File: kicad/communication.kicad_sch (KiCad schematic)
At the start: 34 parts, among them J1 CAN1A, J10 Debug, J2 CAN1B, J6 CAN0A, J7 CAN0B, U13 SK9822-EC20, U15 TJA1462ATK, U8 TJA1462ATK

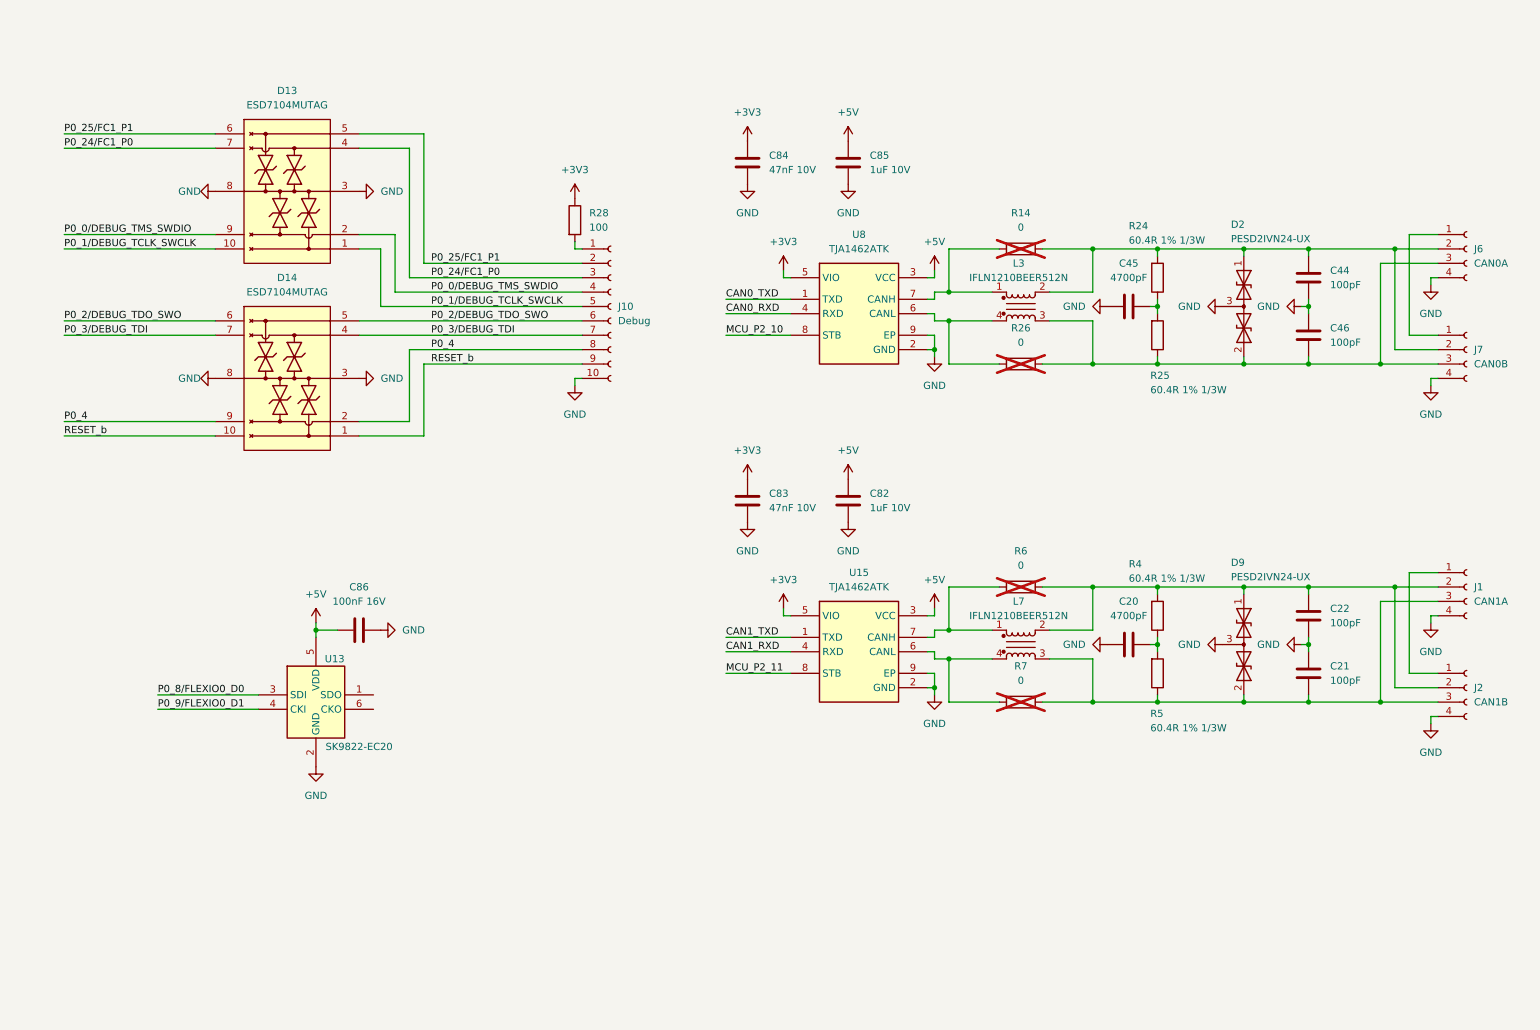
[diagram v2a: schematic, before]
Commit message: Updated schematic and started on layout
- Implemented schematic changes after feedback:
	- BMM350 VDD is 1.8V
	- Replaced net labels with global labels for page references
	- Added 1uF cap to SK9822-EC20
- Added rev-RMII configuration for TJA1103 and DNP resistor to put it in slave mode
- Added TJA1103 PHY address info
- Changed decoupling caps for MCXN to smallest possible packages
- Added traces and vias at MCXN according to guidelines
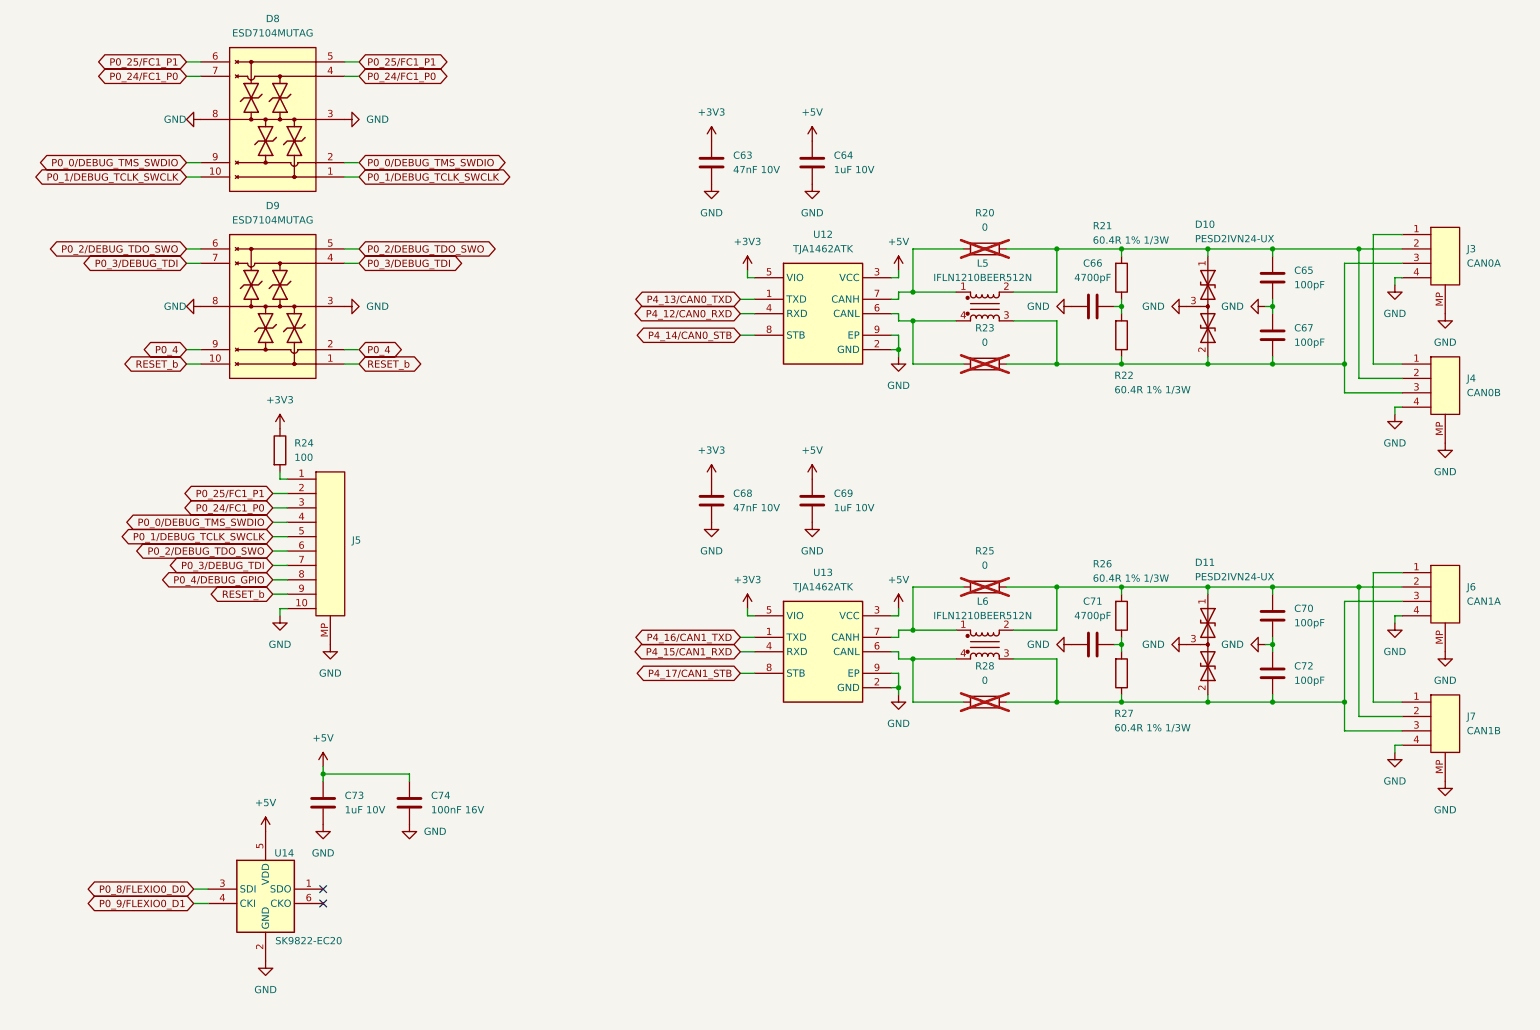
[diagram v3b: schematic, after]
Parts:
- removed J1: CAN1A, Connector_JST:JST_GH_SM04B-GHS-TB_1x04-1MP_P1.25mm_Horizontal, symbol Connector:Conn_01x04_Socket
- removed J10: Debug, Connector_JST:JST_SH_SM10B-SRSS-TB_1x10-1MP_P1.00mm_Horizontal, symbol Connector:Conn_01x10_Socket
- removed J2: CAN1B, Connector_JST:JST_GH_SM04B-GHS-TB_1x04-1MP_P1.25mm_Horizontal, symbol Connector:Conn_01x04_Socket
- removed J6: CAN0A, Connector_JST:JST_GH_SM04B-GHS-TB_1x04-1MP_P1.25mm_Horizontal, symbol Connector:Conn_01x04_Socket
- removed J7: CAN0B, Connector_JST:JST_GH_SM04B-GHS-TB_1x04-1MP_P1.25mm_Horizontal, symbol Connector:Conn_01x04_Socket
- added C73: 1uF 10V, Capacitor_SMD:C_0603_1608Metric, symbol Device:C
- added J3: CAN0A, Connector_JST:JST_GH_SM04B-GHS-TB_1x04-1MP_P1.25mm_Horizontal, symbol Connectors:JST_GH_SM04B-GHS-TB
- added J4: CAN0B, Connector_JST:JST_GH_SM04B-GHS-TB_1x04-1MP_P1.25mm_Horizontal, symbol Connectors:JST_GH_SM04B-GHS-TB
- added J5: ~, Connector_JST:JST_SH_SM10B-SRSS-TB_1x10-1MP_P1.00mm_Horizontal, symbol Connectors:JST_SH_SM10B-SRSS-TB
- added J6: CAN1A, Connector_JST:JST_GH_SM04B-GHS-TB_1x04-1MP_P1.25mm_Horizontal, symbol Connectors:JST_GH_SM04B-GHS-TB
- added J7: CAN1B, Connector_JST:JST_GH_SM04B-GHS-TB_1x04-1MP_P1.25mm_Horizontal, symbol Connectors:JST_GH_SM04B-GHS-TB
- renumbered C84 to C63, C85 to C64, C44 to C65, C45 to C66, C46 to C67, C83 to C68, C82 to C69, C22 to C70, C20 to C71, C21 to C72, C86 to C74, D2 to D10, D9 to D11, D13 to D8, D14 to D9, L3 to L5, L7 to L6, R14 to R20, R24 to R21, R25 to R22, R26 to R23, R28 to R24, R6 to R25, R4 to R26, R5 to R27, R7 to R28, U8 to U12, U15 to U13, U13 to U14
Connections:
- net +5V: now also C74.2, C73.2; no longer C74.1
- net GND: now also C74.1, C73.1, J3.4 (1), J3.MP, J4.4 (1), J4.MP, J5.10 (1), J5.MP, J6.4 (1), J6.MP, J7.4 (1), J7.MP; no longer C74.2
- net P0_0/DEBUG_TMS_SWDIO: now also J5.4 (1)
- net P0_1/DEBUG_TCLK_SWCLK: now also J5.5 (1)
- net P0_24/FC1_P0: now also J5.3 (1)
- net P0_25/FC1_P1: now also J5.2 (1)
- net P0_2/DEBUG_TDO_SWO: now also J5.6 (1)
- net P0_3/DEBUG_TDI: now also J5.7 (1)
- net RESET_b: now also J5.9 (1)
- net at C70.2, D11.1 (A1), L6.2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: now also J6.2 (1), J7.2 (1)
- net at C67.1, D10.2 (A2), L5.3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: now also J3.3 (1), J4.3 (1)
- net at C72.1, D11.2 (A2), L6.3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: now also J6.3 (1), J7.3 (1)
- net at C65.2, D10.1 (A1), L5.2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: now also J3.2 (1), J4.2 (1)
- net at R24.2: now also J5.1
- net CAN0_RXD renamed P4_12/CAN0_RXD
- net CAN0_TXD renamed P4_13/CAN0_TXD
- net CAN1_RXD renamed P4_15/CAN1_RXD
- net CAN1_TXD renamed P4_16/CAN1_TXD
- net MCU_P2_10 renamed P4_14/CAN0_STB
- net MCU_P2_11 renamed P4_17/CAN1_STB
- new net: J3.1, J4.1
- new net: J6.1, J7.1
- new net P0_4/DEBUG_GPIO: J5.8 (1)
- no-connect marks 0 -> 2
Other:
- moved on the sheet: C63, C64, C65, C66, C67, C68, C69, C70, C71, C72, C74, D10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

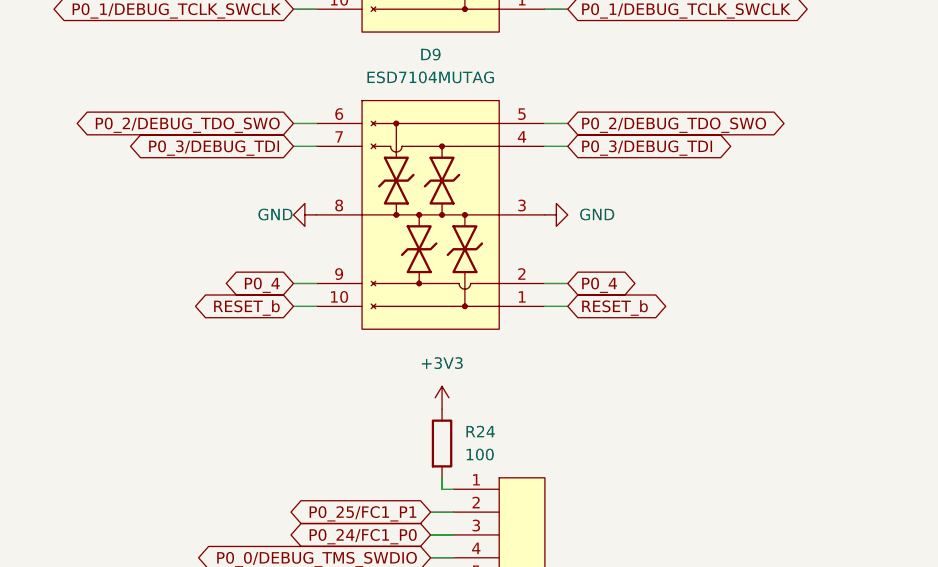
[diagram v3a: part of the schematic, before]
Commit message: Updated PCB layout
- Placed decoupling caps at MCXN with traces.
- Grouped parts of schematic.
- Started positioning Power components
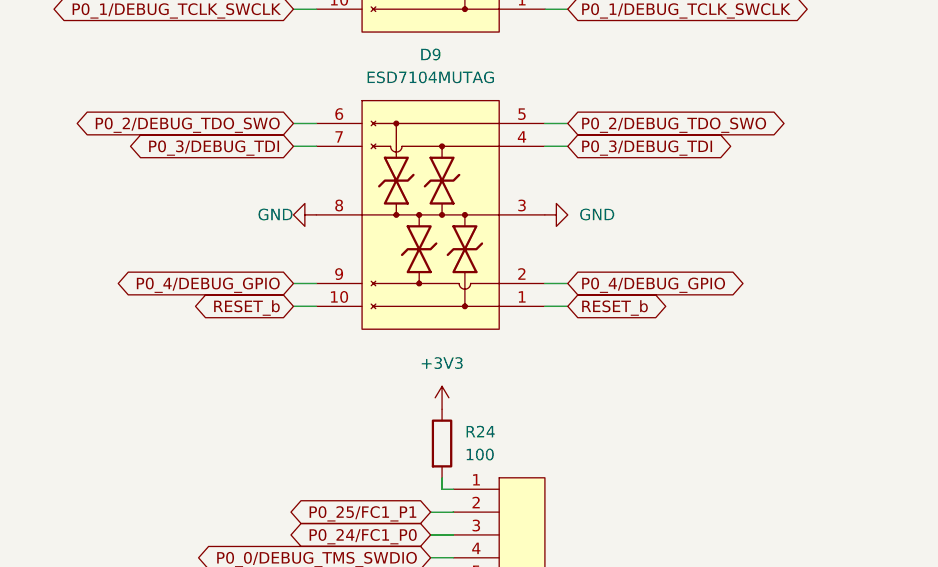
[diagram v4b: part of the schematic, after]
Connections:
- net P0_4 is gone; now on net P0_4/DEBUG_GPIO: D9.2 (IO_2), D9.9 (NC_3)
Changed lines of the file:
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@@
 		)
 	)
-	(global_label "P0_4"
+	(global_label "P4_12{slash}CAN0_RXD"
+		(shape bidirectional)
+		(at 144.78 67.31 180)
+		(fields_autoplaced yes)
+		(effects
+			(font
+				(size 1.27 1.27)
+			)
+			(justify right)
+		)
+		(property "Intersheetrefs" "${INTERSHEET_REFS}"
+			(at 123.8712 67.31 0)
+			(effects
+				(font
+					(size 1.27 1.27)
+				)
+				(justify right)
+			)
+		)
+	)
+	(global_label "P4_15{slash}CAN1_RXD"
+		(shape bidirectional)
+		(at 144.78 127 180)
+		(fields_autoplaced yes)
+		(effects
+			(font
+				(size 1.27 1.27)
+			)
+			(justify right)
+		)
+		(property "Intersheetrefs" "${INTERSHEET_REFS}"
+			(at 123.8712 127 0)
+			(effects
+				(font
+					(size 1.27 1.27)
+				)
+				(justify right)
+			)
+		)
+	)
+	(global_label "P0_4{slash}DEBUG_GPIO"
 		(shape bidirectional)
 		(at 46.99 73.66 180)
@@
 		)
 		(property "Intersheetrefs" "${INTERSHEET_REFS}"
-			(at 38.2369 73.66 0)
-			(effects
-				(font
-					(size 1.27 1.27)
-				)
-				(justify right)
-			)
-		)
-	)
-	(global_label "P4_12{slash}CAN0_RXD"
-		(shape bidirectional)
-		(at 144.78 67.31 180)
-		(fields_autoplaced yes)
-		(effects
-			(font
-				(size 1.27 1.27)
-			)
-			(justify right)
-		)
-		(property "Intersheetrefs" "${INTERSHEET_REFS}"
-			(at 123.8712 67.31 0)
-			(effects
-				(font
-					(size 1.27 1.27)
-				)
-				(justify right)
-			)
-		)
-	)
-	(global_label "P4_15{slash}CAN1_RXD"
-		(shape bidirectional)
-		(at 144.78 127 180)
-		(fields_autoplaced yes)
-		(effects
-			(font
-				(size 1.27 1.27)
-			)
-			(justify right)
-		)
-		(property "Intersheetrefs" "${INTERSHEET_REFS}"
-			(at 123.8712 127 0)
+			(at 25.174 73.66 0)
 			(effects
 				(font
@@
 		)
 	)
-	(global_label "P0_4"
+	(global_label "P0_2{slash}DEBUG_TDO_SWO"
+		(shape bidirectional)
+		(at 62.23 109.22 180)
+		(fields_autoplaced yes)
+		(effects
+			(font
+				(size 1.27 1.27)
+			)
+			(justify right)
+		)
+		(property "Intersheetrefs" "${INTERSHEET_REFS}"
+			(at 36.3622 109.22 0)
+			(effects
+				(font
+					(size 1.27 1.27)
+				)
+				(justify right)
+			)
+		)
+	)
+	(global_label "P0_1{slash}DEBUG_TCLK_SWCLK"
+		(shape bidirectional)
+		(at 46.99 43.18 180)
+		(fields_autoplaced yes)
+		(effects
+			(font
+				(size 1.27 1.27)
+			)
+			(justify right)
+		)
+		(property "Intersheetrefs" "${INTERSHEET_REFS}"
+			(at 17.917 43.18 0)
+			(effects
+				(font
+					(size 1.27 1.27)
+				)
+				(justify right)
+			)
+		)
+	)
+	(global_label "P0_25{slash}FC1_P1"
+		(shape bidirectional)
+		(at 77.47 22.86 0)
+		(fields_autoplaced yes)
+		(effects
+			(font
+				(size 1.27 1.27)
+			)
+			(justify left)
+		)
+		(property "Intersheetrefs" "${INTERSHEET_REFS}"
+			(at 95.7783 22.86 0)
+			(effects
+				(font
+					(size 1.27 1.27)
+				)
+				(justify left)
+			)
+		)
+	)
+	(global_label "P0_3{slash}DEBUG_TDI"
+		(shape bidirectional)
+		(at 62.23 111.76 180)
+		(fields_autoplaced yes)
+		(effects
+			(font
+				(size 1.27 1.27)
+			)
+			(justify right)
+		)
+		(property "Intersheetrefs" "${INTERSHEET_REFS}"
+			(at 42.0469 111.76 0)
+			(effects
+				(font
+					(size 1.27 1.27)
+				)
+				(justify right)
+			)
+		)
+	)
+	(global_label "RESET_b"
+		(shape bidirectional)
+		(at 77.47 76.2 0)
+		(fields_autoplaced yes)
+		(effects
+			(font
+				(size 1.27 1.27)
+			)
+			(justify left)
+		)
+		(property "Intersheetrefs" "${INTERSHEET_REFS}"
+			(at 89.4282 76.2 0)
+			(effects
+				(font
+					(size 1.27 1.27)
+				)
+				(justify left)
+			)
+		)
+	)
+	(global_label "P0_4{slash}DEBUG_GPIO"
 		(shape bidirectional)
 		(at 77.47 73.66 0)
@@
 		)
 		(property "Intersheetrefs" "${INTERSHEET_REFS}"
-			(at 86.2231 73.66 0)
-			(effects
-				(font
-					(size 1.27 1.27)
-				)
-				(justify left)
-			)
-		)
-	)
-	(global_label "P0_2{slash}DEBUG_TDO_SWO"
-		(shape bidirectional)
-		(at 62.23 109.22 180)
-		(fields_autoplaced yes)
-		(effects
-			(font
-				(size 1.27 1.27)
-			)
-			(justify right)
-		)
-		(property "Intersheetrefs" "${INTERSHEET_REFS}"
-			(at 36.3622 109.22 0)
-			(effects
-				(font
-					(size 1.27 1.27)
-				)
-				(justify right)
-			)
-		)
-	)
-	(global_label "P0_1{slash}DEBUG_TCLK_SWCLK"
-		(shape bidirectional)
-		(at 46.99 43.18 180)
-		(fields_autoplaced yes)
-		(effects
-			(font
-				(size 1.27 1.27)
-			)
-			(justify right)
-		)
-		(property "Intersheetrefs" "${INTERSHEET_REFS}"
-			(at 17.917 43.18 0)
-			(effects
-				(font
-					(size 1.27 1.27)
-				)
-				(justify right)
-			)
-		)
-	)
-	(global_label "P0_25{slash}FC1_P1"
-		(shape bidirectional)
-		(at 77.47 22.86 0)
-		(fields_autoplaced yes)
-		(effects
-			(font
-				(size 1.27 1.27)
-			)
-			(justify left)
-		)
-		(property "Intersheetrefs" "${INTERSHEET_REFS}"
-			(at 95.7783 22.86 0)
-			(effects
-				(font
-					(size 1.27 1.27)
-				)
-				(justify left)
-			)
-		)
-	)
-	(global_label "P0_3{slash}DEBUG_TDI"
-		(shape bidirectional)
-		(at 62.23 111.76 180)
-		(fields_autoplaced yes)
-		(effects
-			(font
-				(size 1.27 1.27)
-			)
-			(justify right)
-		)
-		(property "Intersheetrefs" "${INTERSHEET_REFS}"
-			(at 42.0469 111.76 0)
-			(effects
-				(font
-					(size 1.27 1.27)
-				)
-				(justify right)
-			)
-		)
-	)
-	(global_label "RESET_b"
-		(shape bidirectional)
-		(at 77.47 76.2 0)
-		(fields_autoplaced yes)
-		(effects
-			(font
-				(size 1.27 1.27)
-			)
-			(justify left)
-		)
-		(property "Intersheetrefs" "${INTERSHEET_REFS}"
-			(at 89.4282 76.2 0)
-			(effects
-				(font
+			(at 99.286 73.66 0)
+			(effects
+				(font
